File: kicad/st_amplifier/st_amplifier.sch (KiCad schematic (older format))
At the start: 50 parts

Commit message: New commit.
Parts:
- removed C?: 100 п, symbol CAPITORS
- removed C?: 2.2 мк, symbol CAPITORS
- removed R?: 22 к, symbol RESISTOR
- removed XS4: WF-3, ~, symbol PIN_F_3
- removed XS?: WF-2, ~, symbol PIN_F_2
- added C1, C4: 2200мк 50В, symbol CAPITORS_ELECTROLYTIC
- added C12, C13: 10 п, symbol CAPITORS
- added C2, C5: 22мк 35В, symbol CAPITORS_ELECTROLYTIC
- added C22, C23: 0,1 мк, symbol CAPITORS
- added C24: 2.2 мк, symbol CAPITORS
- added C27: 100 п, symbol CAPITORS
- added C3, C6: 0.1 мк, symbol CAPITORS
- added DA1: LM7815, ~, symbol 7815
- added DA2: LM7915, ~, symbol 7915
- added R15, R16: 12 к, symbol RESISTOR
- added R18: 22 к, symbol RESISTOR
- added R19, R4: 2,7 к, symbol RESISTOR
- added R6, R8: 47 к, symbol RESISTOR
- added XS2: WF-4, ~, symbol PIN_F_4
- added XS5: WF-2, ~, symbol PIN_F_2
- C14: renamed from C6; value 1000мк 50В -> 470мк 50В
- C16: renamed from C8; value 1000мк 50В -> 470мк 50В
- C31, C33: renamed from C?; value 1000мк 50В -> 470мк 50В
- DA3: renamed from DA?; value LM258 -> LME49720MA
- R1: value 1 к -> 10 к
- gave numbers to parts that had none: 14
- renumbered C4 to C10, C5 to C11, C7 to C15, C10 to C17, C12 to C18, C13 to C19, C9 to C20, C11 to C21, C1 to C7, C2 to C8, C3 to C9, DA1 to DA4, R7 to R10, R8 to R11, R4 to R5, R5 to R7, R6 to R9, XS2 to XS4
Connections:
- net labels added: +15V, -15V
- wire segments 195 -> 267
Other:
- moved on the sheet: C10, C11, C14, C15, C16, C17, C18, C19, C20, C21, C25, C26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

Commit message: New commit.
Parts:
- C1, C4: value 2200мк 50В -> 470мк 50В
- C14, C16: value 470мк 50В -> 2200мк 50В
- C22, C23: value 0,1 мк -> 0.1 мк
- R1: value 10 к -> 1 к +/-0.5%
- R13: value 1 к -> 1 к +/- 0.5%
- R14: value 27 к -> 2 к +/- 0.5%
- R15, R16: value 12 к -> 12 к +/-0.5%
- R2: value 27 к -> 2 к +/-0.5%
- R6, R8: value 47 к -> 47 к +/-0.5%
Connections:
- wire segments 267 -> 196
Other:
- moved on the sheet: C12, C13

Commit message: New commit.
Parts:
- removed XS5: WF-2, ~, symbol PIN_F_2
- C31, C33: value 470мк 50В -> 2200мк 50В
- XS2: value WF-4 -> WF-5; symbol PIN_F_4 -> PIN_F_5
- XS4: value WF-2 -> WF-4; symbol PIN_F_2 -> PIN_M_4
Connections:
- net labels added: CLIP_1, CLIP_2
- net labels removed: CLIP
- wire segments 196 -> 202
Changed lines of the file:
@@
 Sheet 1 1
 Title ""
-Date "19 apr 2015"
+Date "28 apr 2015"
 Rev ""
 Comp ""
@@
 	8900 5700 8900 6150
 Wire Wire Line
-	11450 4050 11750 4050
+	11450 4050 11800 4050
 Wire Wire Line
 	9850 4400 9650 4400
@@
 	13050 3250 12800 3250
 Wire Wire Line
-	12800 3650 12800 3250
+	12800 3250 12800 3650
 Connection ~ 9750 4050
 Wire Wire Line
@@
 	11850 4850 11850 4750
 Wire Wire Line
-	11550 4750 11850 4750
+	11850 4750 11550 4750
 Connection ~ 11550 4550
 Wire Wire Line
@@
 	2800 5550 4850 5550
 Wire Wire Line
-	2050 5650 2350 5650
-Wire Wire Line
 	3050 5950 3050 6400
 Connection ~ 3050 5550
@@
 	3350 5550 3350 5700
 Wire Wire Line
-	2050 5550 2550 5550
+	1950 5550 2550 5550
 Wire Wire Line
 	3050 6100 3350 6100
@@
 Text Label 8900 6150 1    60   ~ 0
 GND
-Text Label 11750 4050 2    60   ~ 0
-CLIP
+Text Label 11800 4050 2    60   ~ 0
+CLIP_1
 $Comp
 L CAPITORS_ELECTROLYTIC C19
@@
 	1    0    0    -1
 $EndComp
-Text Label 2350 5650 2    60   ~ 0
-GND
-$Comp
-L PIN_F_2 XS4
+$Comp
+L PIN_M_4 XS4
 U 1 1 530320C3
-P 2050 5550
-F 0 "XS4" H 2150 5750 50  0000 L BNN
-F 1 "WF-2" H 2100 5650 50  0000 L BNN
-F 2 "~" H 2500 5700 50  0001 C CNN
-F 3 "" H 2050 5550 60  0001 C CNN
-	1    2050 5550
+P 1850 5950
+F 0 "XS4" H 1950 6150 50  0000 L BNN
+F 1 "WF-4" H 1900 6050 50  0000 L BNN
+F 2 "~" H 2300 6100 50  0001 C CNN
+F 3 "" H 1850 5950 60  0001 C CNN
+	1    1850 5950
 	-1   0    0    -1
 $EndComp
@@
 MU/ST
 Wire Wire Line
-	11250 7600 11550 7600
+	11250 7600 11600 7600
 Wire Wire Line
 	10550 6650 11350 6650
@@
 	12850 6800 12600 6800
 Wire Wire Line
-	12600 7200 12600 6800
+	12600 6800 12600 7200
 Connection ~ 9550 7600
 Wire Wire Line
@@
 	11650 8400 11650 8300
 Wire Wire Line
-	11350 8300 11650 8300
+	11650 8300 11350 8300
 Connection ~ 11350 8100
 Wire Wire Line
@@
 Wire Wire Line
 	13850 7300 14050 7300
-Text Label 11550 7600 2    60   ~ 0
-CLIP
+Text Label 11600 7600 2    60   ~ 0
+CLIP_2
 Text Label 13850 7300 0    60   ~ 0
 GND
@@
 L PIN_F_2 XS?
 U 1 1 552A8688
-P 14050 7200
+P 14050 7300
 AR Path="/52F0D059" Ref="XS?"  Part="1"
 AR Path="/52F0D221" Ref="XS?"  Part="1"
 AR Path="/5303196E" Ref="XS?"  Part="1"
 AR Path="/552A8688" Ref="XS6"  Part="1"
-F 0 "XS6" H 14200 7400 50  0000 L BNN
-F 1 "DG126-5.0-02P-14" H 13900 7300 50  0000 L BNN
-F 2 "~" H 14500 7350 50  0001 C CNN
-F 3 "" H 14050 7200 60  0001 C CNN
-	1    14050 7200
-	1    0    0    -1
+F 0 "XS6" H 14200 6950 50  0000 L BNN
+F 1 "DG126-5.0-02P-14" H 13900 7050 50  0000 L BNN
+F 2 "~" H 14500 7450 50  0001 C CNN
+F 3 "" H 14050 7300 60  0001 C CNN
+	1    14050 7300
+	1    0    0    1
 $EndComp
 Text Label 9350 7600 0    60   ~ 0
@@
 P 11350 8400
 F 0 "C31" V 11450 7950 71  0000 C CNN
-F 1 "470мк 50В" V 11550 7950 71  0000 C CNN
+F 1 "2200мк 50В" V 11550 7950 71  0000 C CNN
 F 2 "" H 11350 8400 60  0001 C CNN
 F 3 "" H 11350 8400 60  0001 C CNN
@@
 P 12200 8800
 F 0 "C33" V 12300 8350 71  0000 C CNN
-F 1 "470мк 50В" V 12400 8350 71  0000 C CNN
+F 1 "2200мк 50В" V 12400 8350 71  0000 C CNN
 F 2 "" H 12200 8800 60  0001 C CNN
 F 3 "" H 12200 8800 60  0001 C CNN
@@
 	2800 6700 3850 6700
 Wire Wire Line
-	2050 6800 2350 6800
-Wire Wire Line
 	3050 7100 3050 7550
 Connection ~ 3050 6700
@@
 	3350 6700 3350 6850
 Wire Wire Line
-	2050 6700 2550 6700
+	1950 6700 2550 6700
 Wire Wire Line
 	3050 7250 3350 7250
@@
 	1    0    0    -1
 $EndComp
-Text Label 2350 6800 2    60   ~ 0
-GND
-$Comp
-L PIN_F_2 XS5
-U 1 1 552A8F0F
-P 2050 6700
-F 0 "XS5" H 2150 6900 50  0000 L BNN
-F 1 "WF-2" H 2100 6800 50  0000 L BNN
-F 2 "~" H 2500 6850 50  0001 C CNN
-F 3 "" H 2050 6700 60  0001 C CNN
-	1    2050 6700
-	-1   0    0    -1
-$EndComp
+Text Label 2150 6050 2    60   ~ 0
+GND
 Wire Wire Line
 	3850 6700 3850 5950
@@
 Connection ~ 6700 6900
 Wire Wire Line
-	2050 2600 2450 2600
-Wire Wire Line
 	2050 2500 2450 2500
-Text Label 2450 2600 2    60   ~ 0
-CLIP
+Wire Wire Line
+	2050 2700 2450 2700
 Text Label 2450 2500 2    60   ~ 0
-GND
-$Comp
-L PIN_F_4 XS?
+CLIP_1
+Text Label 2450 2700 2    60   ~ 0
+GND
+$Comp
+L PIN_F_5 XS?
 U 1 1 552AB154
 P 2050 2300
@@
 AR Path="/552AB154" Ref="XS2"  Part="1"
 F 0 "XS2" H 2150 2500 50  0000 L BNN
-F 1 "WF-4" H 2100 2400 50  0000 L BNN
+F 1 "WF-5" H 2100 2400 50  0000 L BNN
 F 2 "~" H 2500 2450 50  0001 C CNN
 F 3 "" H 2050 2300 60  0001 C CNN
@@
 $EndComp
 Wire Wire Line
-	2050 2400 2450 2400
-Text Label 2450 2400 2    60   ~ 0
+	2050 2300 2450 2300
+Text Label 2450 2300 2    60   ~ 0
 MU/ST
 $Comp
@@
 Connection ~ 6300 1350
 Wire Wire Line
-	2050 2300 2450 2300
-Text Label 2450 2300 2    60   ~ 0
+	2050 2400 2450 2400
+Text Label 2450 2400 2    60   ~ 0
 +29V
+Wire Wire Line
+	1950 6250 1950 6700
+Wire Wire Line
+	1950 5550 1950 5950
+Wire Wire Line
+	1950 5950 1850 5950
+Wire Wire Line
+	1850 6250 1950 6250
+Wire Wire Line
+	1850 6050 2150 6050
+Wire Wire Line
+	1850 6150 1950 6150
+Wire Wire Line
+	1950 6150 1950 6050
+Connection ~ 1950 6050
+Wire Wire Line
+	2050 2600 2450 2600
+Text Label 2450 2600 2    60   ~ 0
+CLIP_1
 $EndSCHEMATC

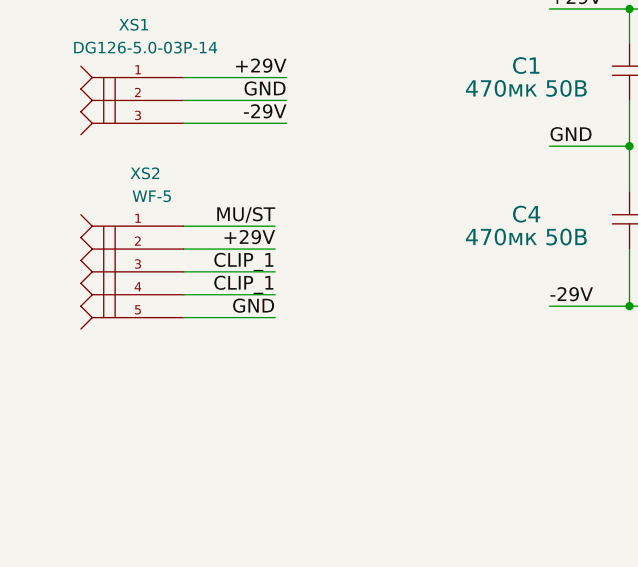
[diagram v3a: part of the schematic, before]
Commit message: Adding board st_amplifier.
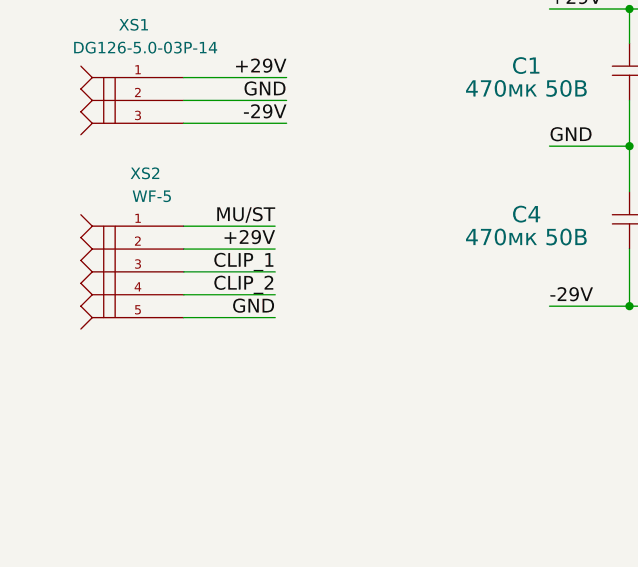
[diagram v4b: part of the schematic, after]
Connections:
- net CLIP_1: no longer XS2.4
- net CLIP_2: now also XS2.4
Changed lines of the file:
@@
 Sheet 1 1
 Title ""
-Date "28 apr 2015"
+Date "29 apr 2015"
 Rev ""
 Comp ""
@@
 	2050 2600 2450 2600
 Text Label 2450 2600 2    60   ~ 0
-CLIP_1
+CLIP_2
 $EndSCHEMATC

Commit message: New commit.
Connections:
- net +29V: now also XS1.2; no longer XS1.1
- net -29V: now also XS1.1; no longer XS1.3
- net GND: now also XS1.3; no longer XS1.2
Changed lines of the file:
@@
 Sheet 1 1
 Title ""
-Date "29 apr 2015"
+Date "1 may 2015"
 Rev ""
 Comp ""
@@
 	0    -1   -1   0
 $EndComp
+Text Label 2500 1650 2    60   ~ 0
+-29V
 Text Label 2500 1850 2    60   ~ 0
--29V
+GND
 Text Label 2500 1750 2    60   ~ 0
-GND
-Text Label 2500 1650 2    60   ~ 0
 +29V
 $Comp

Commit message: New commit.
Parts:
- added R21, R22: 220, symbol RESISTOR
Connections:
- net at C20.2, R12.2: now also R21.1; no longer C21.2, DA3.3 (IN1)
- net at C27.2, DA3.5 (IN2): now also R22.2; no longer C24.2, R18.2
- new net: C21.2, DA3.3 (IN1), R21.2
- new net: C24.2, R18.2, R22.1
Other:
- moved on the sheet: C20, C24, R12, R18
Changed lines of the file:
@@
 Sheet 1 1
 Title ""
-Date "1 may 2015"
+Date "2 may 2015"
 Rev ""
 Comp ""
@@
 Connection ~ 3350 5550
 Wire Wire Line
-	2800 5550 4850 5550
-Wire Wire Line
-	3050 5950 3050 6400
-Connection ~ 3050 5550
-Wire Wire Line
-	3050 5700 3050 5550
+	2400 5550 2850 5550
+Wire Wire Line
+	3100 5550 4850 5550
+Wire Wire Line
+	2650 5950 2650 6400
+Connection ~ 2650 5550
+Wire Wire Line
+	2650 5550 2650 5700
 Wire Wire Line
 	3350 5550 3350 5700
 Wire Wire Line
-	1950 5550 2550 5550
-Wire Wire Line
-	3050 6100 3350 6100
+	1950 5550 2150 5550
+Wire Wire Line
+	2650 6100 3350 6100
 Wire Wire Line
 	3350 6100 3350 5950
-Connection ~ 3050 6100
+Connection ~ 2650 6100
 Wire Wire Line
 	11550 4450 11450 4450
@@
 	1    0    0    -1
 $EndComp
-Text Label 3050 6400 1    60   ~ 0
+Text Label 2650 6400 1    60   ~ 0
 GND
 $Comp
 L RESISTOR R12
 U 1 1 53032164
-P 3050 5950
-F 0 "R12" V 3250 6150 71  0000 C CNN
-F 1 "22 к" V 3100 6150 71  0000 C CNN
-F 2 "" H 3050 5950 60  0001 C CNN
-F 3 "" H 3050 5950 60  0001 C CNN
-	1    3050 5950
+P 2650 5950
+F 0 "R12" V 2850 6150 71  0000 C CNN
+F 1 "22 к" V 2700 6150 71  0000 C CNN
+F 2 "" H 2650 5950 60  0001 C CNN
+F 3 "" H 2650 5950 60  0001 C CNN
+	1    2650 5950
 	0    -1   -1   0
 $EndComp
@@
 L CAPITORS C20
 U 1 1 53032103
-P 2550 5550
-F 0 "C20" H 2500 5700 71  0000 C CNN
-F 1 "2.2 мк" H 2850 5700 71  0000 C CNN
-F 2 "" H 2550 5550 60  0001 C CNN
-F 3 "" H 2550 5550 60  0001 C CNN
-	1    2550 5550
+P 2150 5550
+F 0 "C20" H 2100 5700 71  0000 C CNN
+F 1 "2.2 мк" H 2450 5700 71  0000 C CNN
+F 2 "" H 2150 5550 60  0001 C CNN
+F 3 "" H 2150 5550 60  0001 C CNN
+	1    2150 5550
 	1    0    0    -1
 $EndComp
@@
 Connection ~ 3350 6700
 Wire Wire Line
-	2800 6700 3850 6700
-Wire Wire Line
-	3050 7100 3050 7550
-Connection ~ 3050 6700
-Wire Wire Line
-	3050 6850 3050 6700
+	2400 6700 2850 6700
+Wire Wire Line
+	3100 6700 3850 6700
+Wire Wire Line
+	2650 7100 2650 7550
+Connection ~ 2650 6700
+Wire Wire Line
+	2650 6700 2650 6850
 Wire Wire Line
 	3350 6700 3350 6850
 Wire Wire Line
-	1950 6700 2550 6700
-Wire Wire Line
-	3050 7250 3350 7250
+	1950 6700 2150 6700
+Wire Wire Line
+	2650 7250 3350 7250
 Wire Wire Line
 	3350 7250 3350 7100
-Connection ~ 3050 7250
-Text Label 3050 7550 1    60   ~ 0
+Connection ~ 2650 7250
+Text Label 2650 7550 1    60   ~ 0
 GND
 $Comp
 L RESISTOR R18
 U 1 1 552A8EFC
-P 3050 7100
-F 0 "R18" V 3250 7300 71  0000 C CNN
-F 1 "22 к" V 3100 7300 71  0000 C CNN
-F 2 "" H 3050 7100 60  0001 C CNN
-F 3 "" H 3050 7100 60  0001 C CNN
-	1    3050 7100
+P 2650 7100
+F 0 "R18" V 2850 7300 71  0000 C CNN
+F 1 "22 к" V 2700 7300 71  0000 C CNN
+F 2 "" H 2650 7100 60  0001 C CNN
+F 3 "" H 2650 7100 60  0001 C CNN
+	1    2650 7100
 	0    -1   -1   0
 $EndComp
@@
 L CAPITORS C24
 U 1 1 552A8F08
-P 2550 6700
-F 0 "C24" H 2500 6850 71  0000 C CNN
-F 1 "2.2 мк" H 2850 6850 71  0000 C CNN
-F 2 "" H 2550 6700 60  0001 C CNN
-F 3 "" H 2550 6700 60  0001 C CNN
-	1    2550 6700
+P 2150 6700
+F 0 "C24" H 2100 6850 71  0000 C CNN
+F 1 "2.2 мк" H 2450 6850 71  0000 C CNN
+F 2 "" H 2150 6700 60  0001 C CNN
+F 3 "" H 2150 6700 60  0001 C CNN
+	1    2150 6700
 	1    0    0    -1
 $EndComp
@@
 Text Label 2450 2600 2    60   ~ 0
 CLIP_2
+$Comp
+L RESISTOR R21
+U 1 1 55449D1F
+P 2850 5550
+F 0 "R21" H 2850 5700 71  0000 C CNN
+F 1 "220" H 3150 5700 71  0000 C CNN
+F 2 "" H 2850 5550 60  0001 C CNN
+F 3 "" H 2850 5550 60  0001 C CNN
+	1    2850 5550
+	1    0    0    -1
+$EndComp
+$Comp
+L RESISTOR R22
+U 1 1 55449FB2
+P 2850 6700
+F 0 "R22" H 2850 6850 71  0000 C CNN
+F 1 "220" H 3150 6850 71  0000 C CNN
+F 2 "" H 2850 6700 60  0001 C CNN
+F 3 "" H 2850 6700 60  0001 C CNN
+	1    2850 6700
+	1    0    0    -1
+$EndComp
 $EndSCHEMATC

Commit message: New commit.
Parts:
- removed R21, R22: 220, symbol RESISTOR
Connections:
- net at C20.2, R12.2: now also C21.2, DA3.3 (IN1)
- net at C27.2, DA3.5 (IN2): now also C24.2, R18.2
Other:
- moved on the sheet: C20, C24, R12, R18, XS4
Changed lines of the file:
@@
 Sheet 1 1
 Title ""
-Date "2 may 2015"
+Date "3 may 2015"
 Rev ""
 Comp ""
@@
 	13050 3250 12800 3250
 Wire Wire Line
-	12800 3250 12800 3650
+	12800 3650 12800 3250
 Connection ~ 9750 4050
 Wire Wire Line
@@
 	11850 4850 11850 4750
 Wire Wire Line
-	11850 4750 11550 4750
+	11550 4750 11850 4750
 Connection ~ 11550 4550
 Wire Wire Line
@@
 Connection ~ 3350 5550
 Wire Wire Line
-	2400 5550 2850 5550
-Wire Wire Line
-	3100 5550 4850 5550
-Wire Wire Line
-	2650 5950 2650 6400
-Connection ~ 2650 5550
-Wire Wire Line
-	2650 5550 2650 5700
+	2850 5550 4850 5550
+Wire Wire Line
+	3100 5950 3100 6400
+Connection ~ 3100 5550
+Wire Wire Line
+	3100 5550 3100 5700
 Wire Wire Line
 	3350 5550 3350 5700
 Wire Wire Line
-	1950 5550 2150 5550
-Wire Wire Line
-	2650 6100 3350 6100
+	2400 5550 2600 5550
+Wire Wire Line
+	3100 6100 3350 6100
 Wire Wire Line
 	3350 6100 3350 5950
-Connection ~ 2650 6100
+Connection ~ 3100 6100
 Wire Wire Line
 	11550 4450 11450 4450
@@
 	1    0    0    -1
 $EndComp
-Text Label 2650 6400 1    60   ~ 0
+Text Label 3100 6400 1    60   ~ 0
 GND
 $Comp
 L RESISTOR R12
 U 1 1 53032164
-P 2650 5950
-F 0 "R12" V 2850 6150 71  0000 C CNN
-F 1 "22 к" V 2700 6150 71  0000 C CNN
-F 2 "" H 2650 5950 60  0001 C CNN
-F 3 "" H 2650 5950 60  0001 C CNN
-	1    2650 5950
+P 3100 5950
+F 0 "R12" V 3300 6150 71  0000 C CNN
+F 1 "22 к" V 3150 6150 71  0000 C CNN
+F 2 "" H 3100 5950 60  0001 C CNN
+F 3 "" H 3100 5950 60  0001 C CNN
+	1    3100 5950
 	0    -1   -1   0
 $EndComp
@@
 L CAPITORS C20
 U 1 1 53032103
-P 2150 5550
-F 0 "C20" H 2100 5700 71  0000 C CNN
-F 1 "2.2 мк" H 2450 5700 71  0000 C CNN
-F 2 "" H 2150 5550 60  0001 C CNN
-F 3 "" H 2150 5550 60  0001 C CNN
-	1    2150 5550
+P 2600 5550
+F 0 "C20" H 2550 5700 71  0000 C CNN
+F 1 "2.2 мк" H 2900 5700 71  0000 C CNN
+F 2 "" H 2600 5550 60  0001 C CNN
+F 3 "" H 2600 5550 60  0001 C CNN
+	1    2600 5550
 	1    0    0    -1
 $EndComp
@@
 L PIN_M_4 XS4
 U 1 1 530320C3
-P 1850 5950
-F 0 "XS4" H 1950 6150 50  0000 L BNN
-F 1 "WF-4" H 1900 6050 50  0000 L BNN
-F 2 "~" H 2300 6100 50  0001 C CNN
-F 3 "" H 1850 5950 60  0001 C CNN
-	1    1850 5950
+P 2300 5950
+F 0 "XS4" H 2400 6150 50  0000 L BNN
+F 1 "WF-4" H 2350 6050 50  0000 L BNN
+F 2 "~" H 2750 6100 50  0001 C CNN
+F 3 "" H 2300 5950 60  0001 C CNN
+	1    2300 5950
 	-1   0    0    -1
 $EndComp
@@
 	12850 6800 12600 6800
 Wire Wire Line
-	12600 6800 12600 7200
+	12600 7200 12600 6800
 Connection ~ 9550 7600
 Wire Wire Line
@@
 	11650 8400 11650 8300
 Wire Wire Line
-	11650 8300 11350 8300
+	11350 8300 11650 8300
 Connection ~ 11350 8100
 Wire Wire Line
@@
 Connection ~ 3350 6700
 Wire Wire Line
-	2400 6700 2850 6700
-Wire Wire Line
-	3100 6700 3850 6700
-Wire Wire Line
-	2650 7100 2650 7550
-Connection ~ 2650 6700
-Wire Wire Line
-	2650 6700 2650 6850
+	2850 6700 3850 6700
+Wire Wire Line
+	3100 7100 3100 7550
+Connection ~ 3100 6700
+Wire Wire Line
+	3100 6700 3100 6850
 Wire Wire Line
 	3350 6700 3350 6850
 Wire Wire Line
-	1950 6700 2150 6700
-Wire Wire Line
-	2650 7250 3350 7250
+	2400 6700 2600 6700
+Wire Wire Line
+	3100 7250 3350 7250
 Wire Wire Line
 	3350 7250 3350 7100
-Connection ~ 2650 7250
-Text Label 2650 7550 1    60   ~ 0
+Connection ~ 3100 7250
+Text Label 3100 7550 1    60   ~ 0
 GND
 $Comp
 L RESISTOR R18
 U 1 1 552A8EFC
-P 2650 7100
-F 0 "R18" V 2850 7300 71  0000 C CNN
-F 1 "22 к" V 2700 7300 71  0000 C CNN
-F 2 "" H 2650 7100 60  0001 C CNN
-F 3 "" H 2650 7100 60  0001 C CNN
-	1    2650 7100
+P 3100 7100
+F 0 "R18" V 3300 7300 71  0000 C CNN
+F 1 "22 к" V 3150 7300 71  0000 C CNN
+F 2 "" H 3100 7100 60  0001 C CNN
+F 3 "" H 3100 7100 60  0001 C CNN
+	1    3100 7100
 	0    -1   -1   0
 $EndComp
@@
 L CAPITORS C24
 U 1 1 552A8F08
-P 2150 6700
-F 0 "C24" H 2100 6850 71  0000 C CNN
-F 1 "2.2 мк" H 2450 6850 71  0000 C CNN
-F 2 "" H 2150 6700 60  0001 C CNN
-F 3 "" H 2150 6700 60  0001 C CNN
-	1    2150 6700
-	1    0    0    -1
-$EndComp
-Text Label 2150 6050 2    60   ~ 0
+P 2600 6700
+F 0 "C24" H 2550 6850 71  0000 C CNN
+F 1 "2.2 мк" H 2900 6850 71  0000 C CNN
+F 2 "" H 2600 6700 60  0001 C CNN
+F 3 "" H 2600 6700 60  0001 C CNN
+	1    2600 6700
+	1    0    0    -1
+$EndComp
+Text Label 2600 6050 2    60   ~ 0
 GND
 Wire Wire Line
@@
 +29V
 Wire Wire Line
-	1950 6250 1950 6700
-Wire Wire Line
-	1950 5550 1950 5950
-Wire Wire Line
-	1950 5950 1850 5950
-Wire Wire Line
-	1850 6250 1950 6250
-Wire Wire Line
-	1850 6050 2150 6050
-Wire Wire Line
-	1850 6150 1950 6150
-Wire Wire Line
-	1950 6150 1950 6050
-Connection ~ 1950 6050
+	2400 6250 2400 6700
+Wire Wire Line
+	2400 5550 2400 5950
+Wire Wire Line
+	2400 5950 2300 5950
+Wire Wire Line
+	2300 6250 2400 6250
+Wire Wire Line
+	2300 6050 2600 6050
+Wire Wire Line
+	2300 6150 2400 6150
+Wire Wire Line
+	2400 6150 2400 6050
+Connection ~ 2400 6050
 Wire Wire Line
 	2050 2600 2450 2600
 Text Label 2450 2600 2    60   ~ 0
 CLIP_2
-$Comp
-L RESISTOR R21
-U 1 1 55449D1F
-P 2850 5550
-F 0 "R21" H 2850 5700 71  0000 C CNN
-F 1 "220" H 3150 5700 71  0000 C CNN
-F 2 "" H 2850 5550 60  0001 C CNN
-F 3 "" H 2850 5550 60  0001 C CNN
-	1    2850 5550
-	1    0    0    -1
-$EndComp
-$Comp
-L RESISTOR R22
-U 1 1 55449FB2
-P 2850 6700
-F 0 "R22" H 2850 6850 71  0000 C CNN
-F 1 "220" H 3150 6850 71  0000 C CNN
-F 2 "" H 2850 6700 60  0001 C CNN
-F 3 "" H 2850 6700 60  0001 C CNN
-	1    2850 6700
-	1    0    0    -1
-$EndComp
 $EndSCHEMATC
